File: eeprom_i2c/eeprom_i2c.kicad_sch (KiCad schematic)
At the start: 7 parts, among them J1 Conn_01x03_Pin, J2 Conn_01x03_Pin, J3 Conn_01x03_Pin, J4 1x4 strip 2.54mm, U1 24LC256

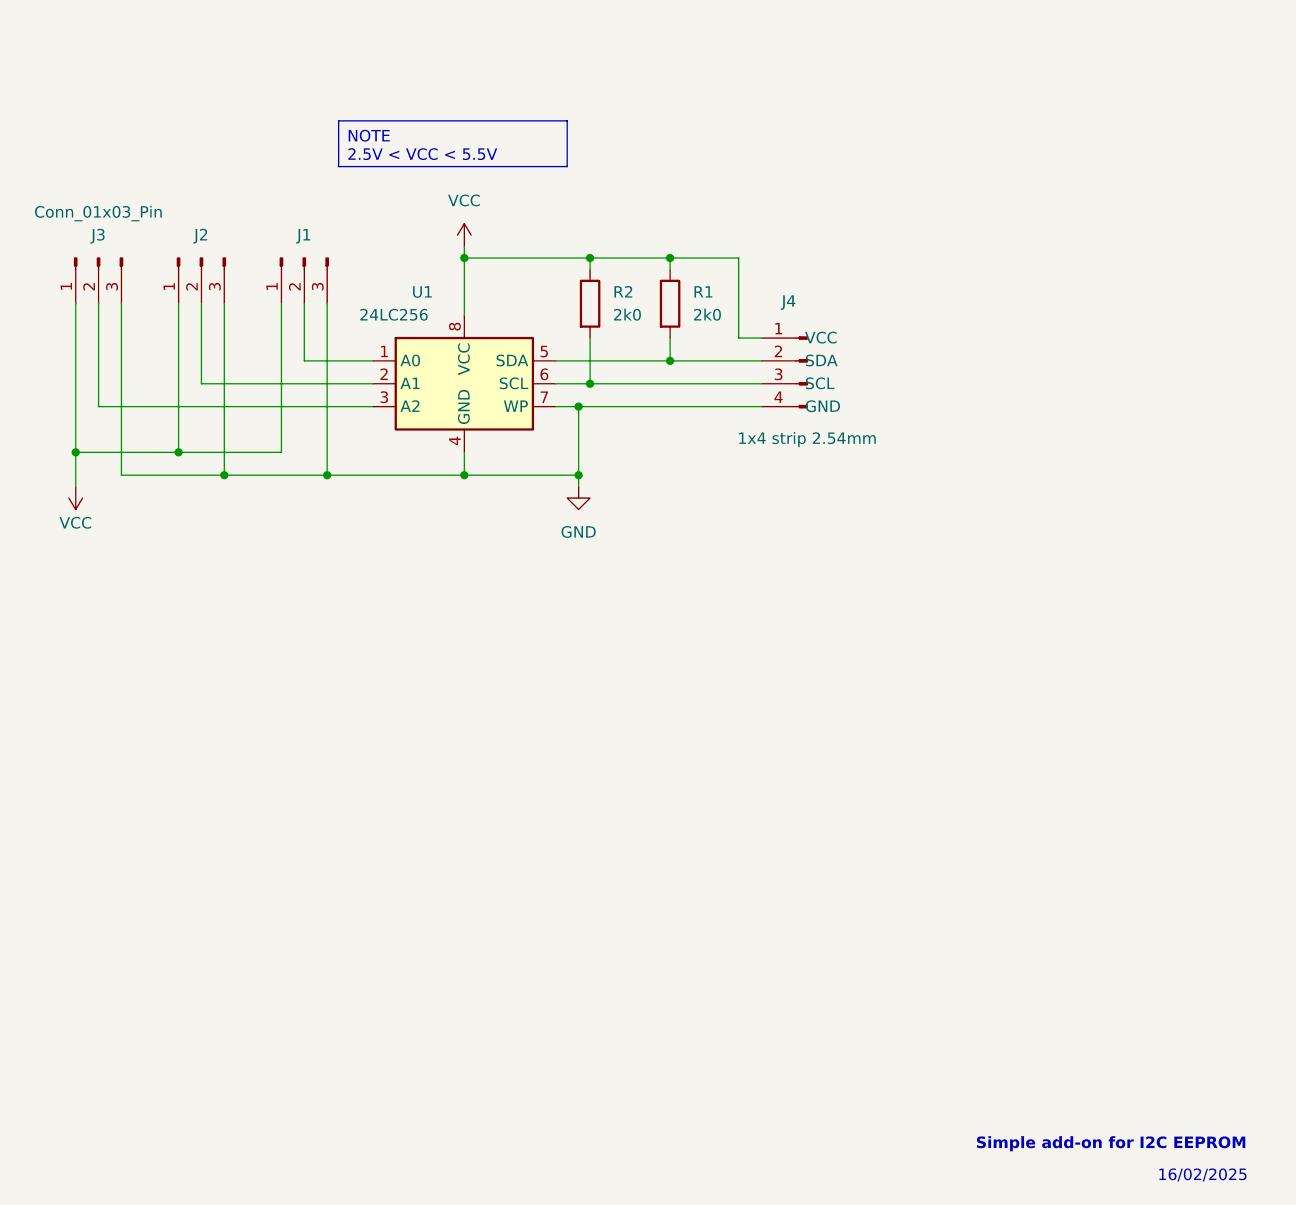
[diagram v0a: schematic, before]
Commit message: Add by-pass capacitor; add mounting hole and change main connector's pinout.
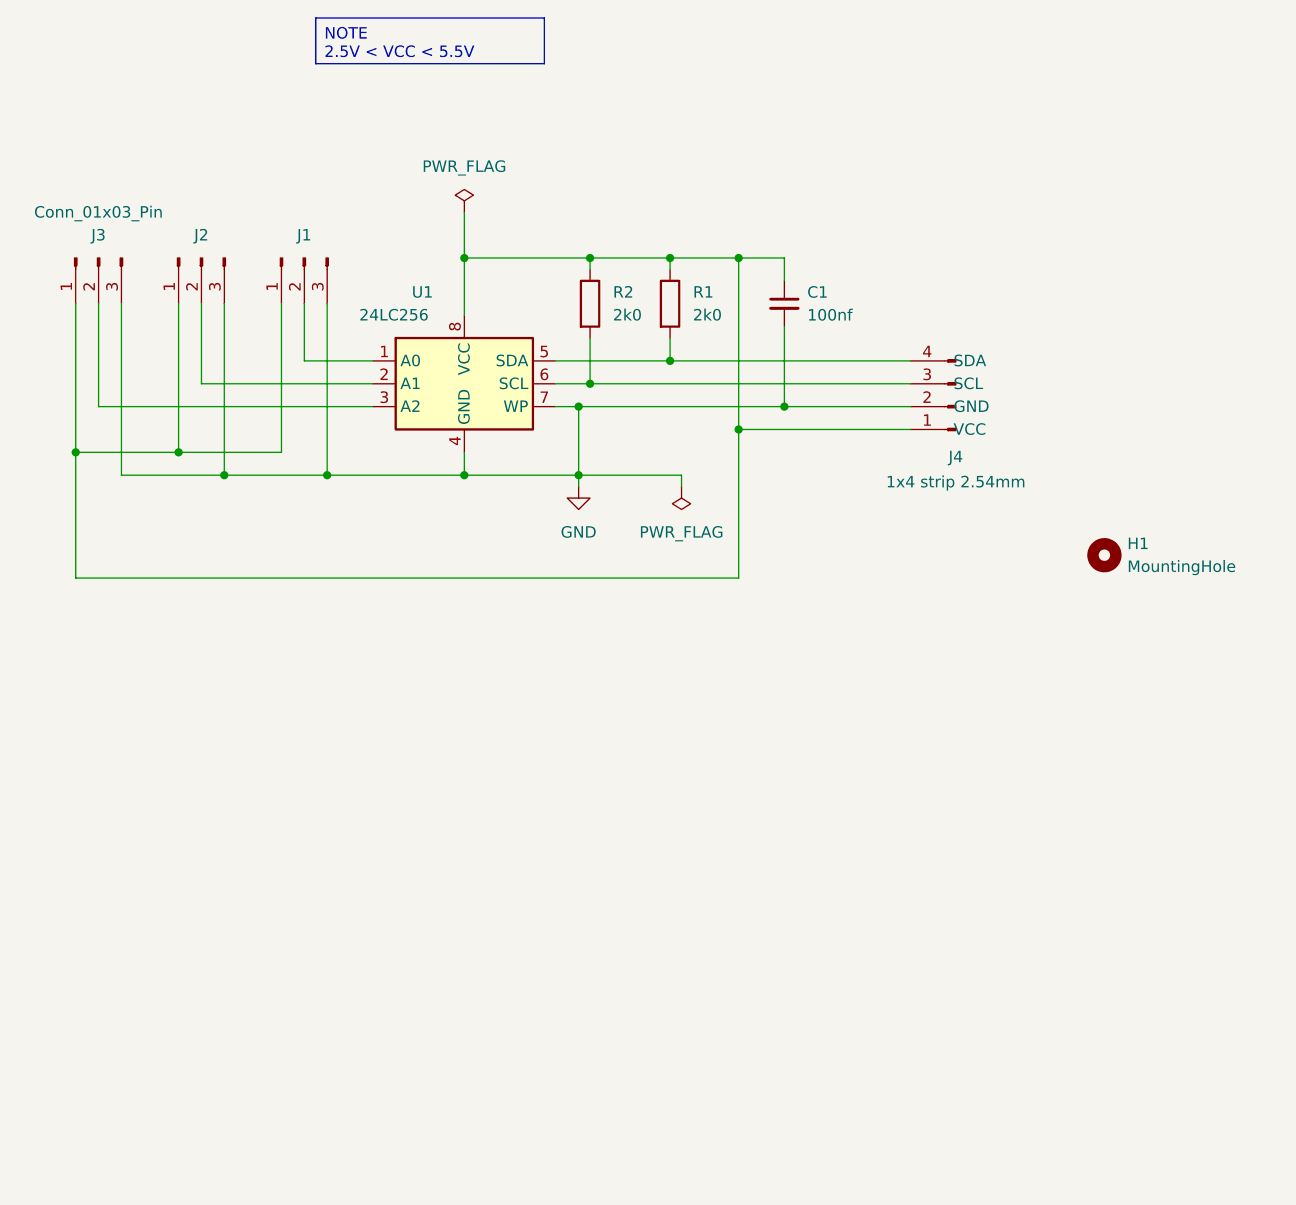
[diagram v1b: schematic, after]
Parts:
- added C1: 100nf, Capacitor_THT:C_Disc_D3.0mm_W2.0mm_P2.50mm, symbol Device:C_Small
- added H1: MountingHole, MountingHole:MountingHole_3.2mm_M3, symbol Mechanical:MountingHole
- J4: footprint Connector_PinSocket_2.54mm:PinSocket_1x04_P2.54mm_Vertical -> Connector_PinHeader_2.54mm:PinHeader_1x04_P2.54mm_Vertical
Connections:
- net GND: now also J4.2 (GND), C1.2; no longer J4.4 (GND)
- net at R1.2, U1.5 (SDA): now also J4.4 (SDA); no longer J4.2 (SDA)
- net VCC: no longer names the net of J1.1 (Pin_1), J2.1 (Pin_1), J3.1 (Pin_1), J4.1 (VCC), R1.1, R2.1, U1.8 (VCC)
- net VCC: now also C1.1
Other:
- note removed: "16/02/2025"
- note removed: "Simple add-on for I2C EEPROM"
- company: (none) -> AM
- title: (none) -> Simple add-on for I2C EEPROM
- moved on the sheet: J4
